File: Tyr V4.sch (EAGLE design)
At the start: 190 parts, among them J1 TYR_TYR_DISPLAY, U1 TYR_ATMEGA32U4, U2 CONTROLLER_PRTR5V0U2X, U4 TYR_TPS2552, X1 CONTROLLER_USB-C-12PUSB-C-12P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, Y1 16Mhz

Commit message: Update pads
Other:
- moved on the sheet: X1

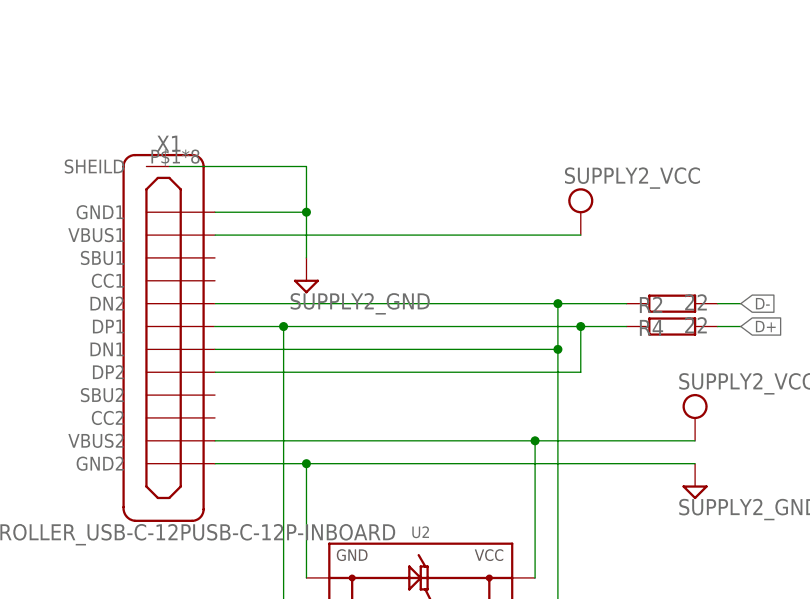
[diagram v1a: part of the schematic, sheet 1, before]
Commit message: Added Type-C CC pulldown resistors
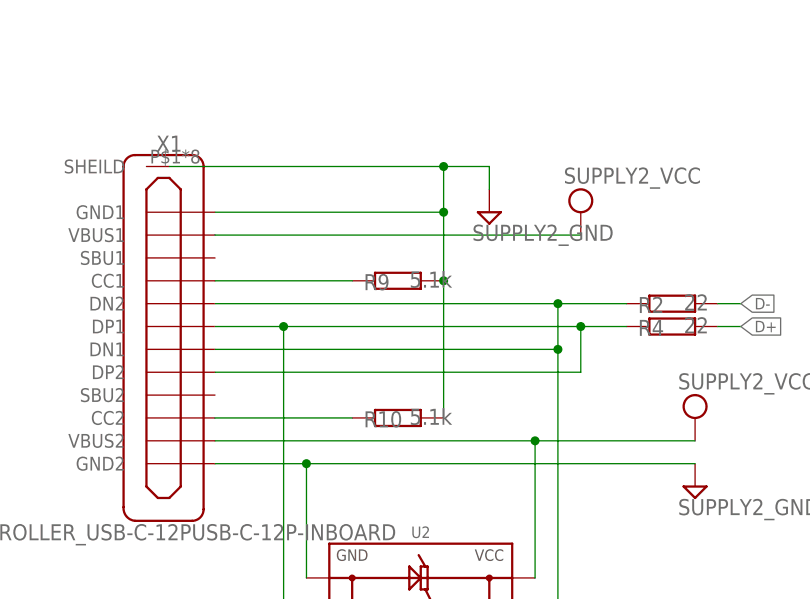
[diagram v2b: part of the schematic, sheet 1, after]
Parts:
- added R10, R9: 5.1k, Tyr V4:COMPONENTS_RESISTOR-0603
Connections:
- new net N$4: R9.1, X1.CC1
- new net N$89: R10.1, X1.CC2
- net GND: now also R10.2, R9.2
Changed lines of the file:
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@@
 <part name="SUPPLY18" library="Tyr V4" deviceset="SUPPLY2_GND" device=""/>
 <part name="FRAME1" library="Tyr V4" deviceset="FRAMES_A3L-LOC" device=""/>
-<part name="SUPPLY4" library="Tyr V4" deviceset="SUPPLY2_GND" device=""/>
 <part name="FRAME2" library="Tyr V4" deviceset="FRAMES_A3L-LOC" device=""/>
 <part name="FRAME3" library="Tyr V4" deviceset="FRAMES_A3L-LOC" device=""/>
@@
 <part name="SUPPLY98" library="Tyr V4" deviceset="SUPPLY2_GND" device=""/>
 <part name="R8" library="Tyr V4" deviceset="COMPONENTS_RESISTOR" device="-0603" value="100k"/>
+<part name="R9" library="Tyr V4" deviceset="COMPONENTS_RESISTOR" device="-0603" value="5.1k"/>
+<part name="R10" library="Tyr V4" deviceset="COMPONENTS_RESISTOR" device="-0603" value="5.1k"/>
+<part name="SUPPLY4" library="Tyr V4" deviceset="SUPPLY2_GND" device=""/>
 </parts>
 <sheets>
@@
 <attribute name="SHEET" x="357.505" y="5.08" size="2.54" layer="94"/>
 </instance>
-<instance part="SUPPLY4" gate="GND" x="246.38" y="193.04" smashed="yes">
-<attribute name="VALUE" x="244.475" y="189.865" size="1.778" layer="96"/>
-</instance>
 <instance part="R7" gate="G$1" x="149.86" y="53.34" smashed="yes" rot="R90">
 <attribute name="NAME" x="148.3614" y="52.07" size="1.778" layer="95" rot="R90"/>
@@
 <attribute name="NAME" x="148.3614" y="87.63" size="1.778" layer="95" rot="R90"/>
 <attribute name="VALUE" x="153.416" y="86.614" size="1.778" layer="96" rot="R90"/>
+</instance>
+<instance part="R9" gate="G$1" x="256.54" y="193.04" smashed="yes">
+<attribute name="NAME" x="252.73" y="191.9986" size="1.778" layer="95"/>
+<attribute name="VALUE" x="257.81" y="192.278" size="1.778" layer="96"/>
+</instance>
+<instance part="R10" gate="G$1" x="256.54" y="177.8" smashed="yes">
+<attribute name="NAME" x="252.73" y="176.7586" size="1.778" layer="95"/>
+<attribute name="VALUE" x="257.81" y="177.038" size="1.778" layer="96"/>
+</instance>
+<instance part="SUPPLY4" gate="GND" x="266.7" y="200.66" smashed="yes">
+<attribute name="VALUE" x="264.795" y="197.485" size="1.778" layer="96"/>
 </instance>
 </instances>
@@
 </segment>
 <segment>
-<pinref part="X1" gate="G$1" pin="GND1"/>
-<wire x1="236.22" y1="200.66" x2="246.38" y2="200.66" width="0.1524" layer="91"/>
-<wire x1="246.38" y1="200.66" x2="246.38" y2="195.58" width="0.1524" layer="91"/>
-<pinref part="SUPPLY4" gate="GND" pin="GND"/>
-<pinref part="X1" gate="G$1" pin="SHEILD"/>
-<wire x1="231.14" y1="205.74" x2="246.38" y2="205.74" width="0.1524" layer="91"/>
-<wire x1="246.38" y1="205.74" x2="246.38" y2="200.66" width="0.1524" layer="91"/>
-<junction x="246.38" y="200.66"/>
-</segment>
-<segment>
 <pinref part="R7" gate="G$1" pin="1"/>
 <pinref part="SUPPLY20" gate="GND" pin="GND"/>
@@
 <wire x1="353.06" y1="27.94" x2="347.98" y2="27.94" width="0.1524" layer="91"/>
 <pinref part="SUPPLY97" gate="GND" pin="GND"/>
+</segment>
+<segment>
+<pinref part="R10" gate="G$1" pin="2"/>
+<pinref part="R9" gate="G$1" pin="2"/>
+<wire x1="261.62" y1="177.8" x2="261.62" y2="193.04" width="0.1524" layer="91"/>
+<pinref part="X1" gate="G$1" pin="GND1"/>
+<wire x1="236.22" y1="200.66" x2="261.62" y2="200.66" width="0.1524" layer="91"/>
+<pinref part="X1" gate="G$1" pin="SHEILD"/>
+<wire x1="231.14" y1="205.74" x2="261.62" y2="205.74" width="0.1524" layer="91"/>
+<wire x1="261.62" y1="205.74" x2="261.62" y2="200.66" width="0.1524" layer="91"/>
+<wire x1="261.62" y1="193.04" x2="261.62" y2="200.66" width="0.1524" layer="91"/>
+<junction x="261.62" y="193.04"/>
+<junction x="261.62" y="200.66"/>
+<wire x1="261.62" y1="205.74" x2="266.7" y2="205.74" width="0.1524" layer="91"/>
+<wire x1="266.7" y1="205.74" x2="266.7" y2="203.2" width="0.1524" layer="91"/>
+<junction x="261.62" y="205.74"/>
+<pinref part="SUPPLY4" gate="GND" pin="GND"/>
 </segment>
 </net>
@@
 </segment>
 </net>
+<net name="N$4" class="0">
+<segment>
+<pinref part="X1" gate="G$1" pin="CC1"/>
+<pinref part="R9" gate="G$1" pin="1"/>
+<wire x1="236.22" y1="193.04" x2="251.46" y2="193.04" width="0.1524" layer="91"/>
+</segment>
+</net>
+<net name="N$89" class="0">
+<segment>
+<pinref part="X1" gate="G$1" pin="CC2"/>
+<pinref part="R10" gate="G$1" pin="1"/>
+<wire x1="236.22" y1="177.8" x2="251.46" y2="177.8" width="0.1524" layer="91"/>
+</segment>
+</net>
